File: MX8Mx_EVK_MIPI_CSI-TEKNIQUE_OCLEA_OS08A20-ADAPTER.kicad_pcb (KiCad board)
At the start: 2 copper layers, 40.6 x 40.2 mm, 11 parts, among them J1 1888863-4, J2 XF2M-3215-1A, U1 NLSX5014DTR2G, U2 SN74LVC1G14DRL

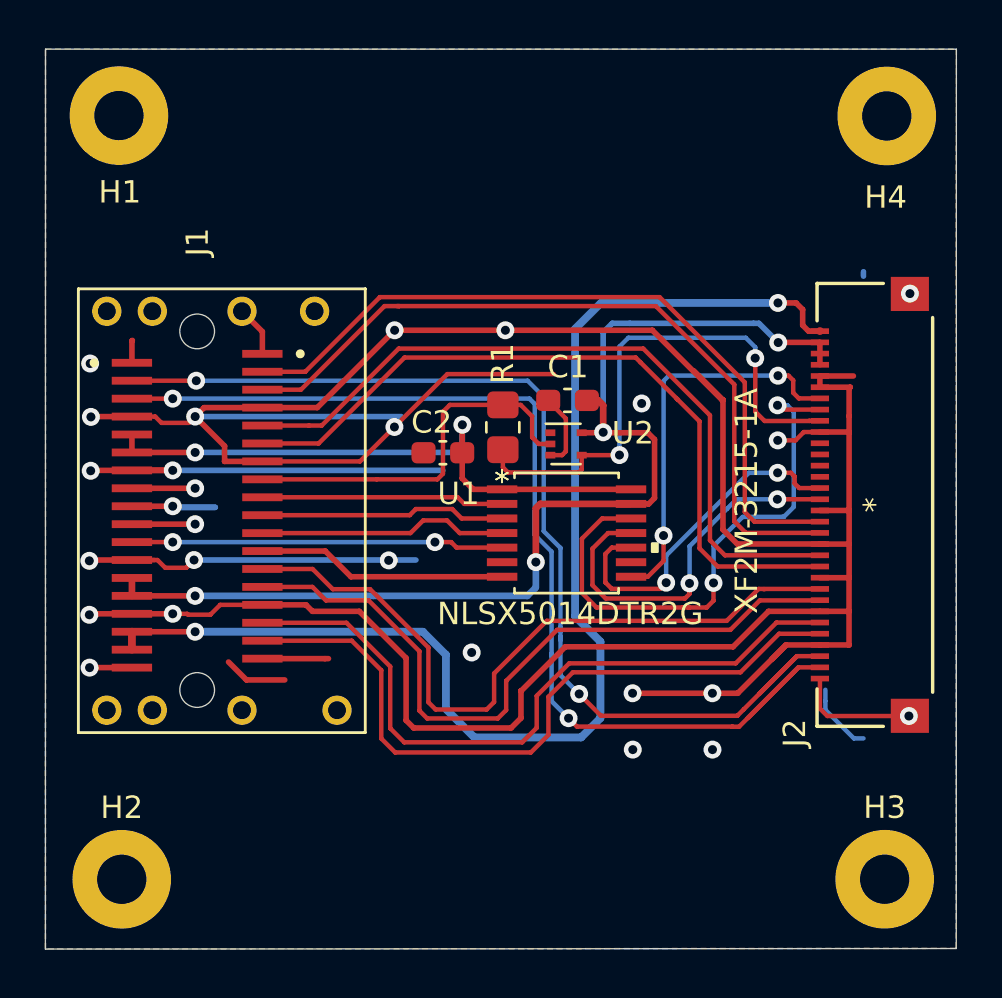
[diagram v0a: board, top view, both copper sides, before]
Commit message: Mirror J1 signals (A-side to B-side and vice-versa) for mating with the MIPI-CSI interface(s) on EVK
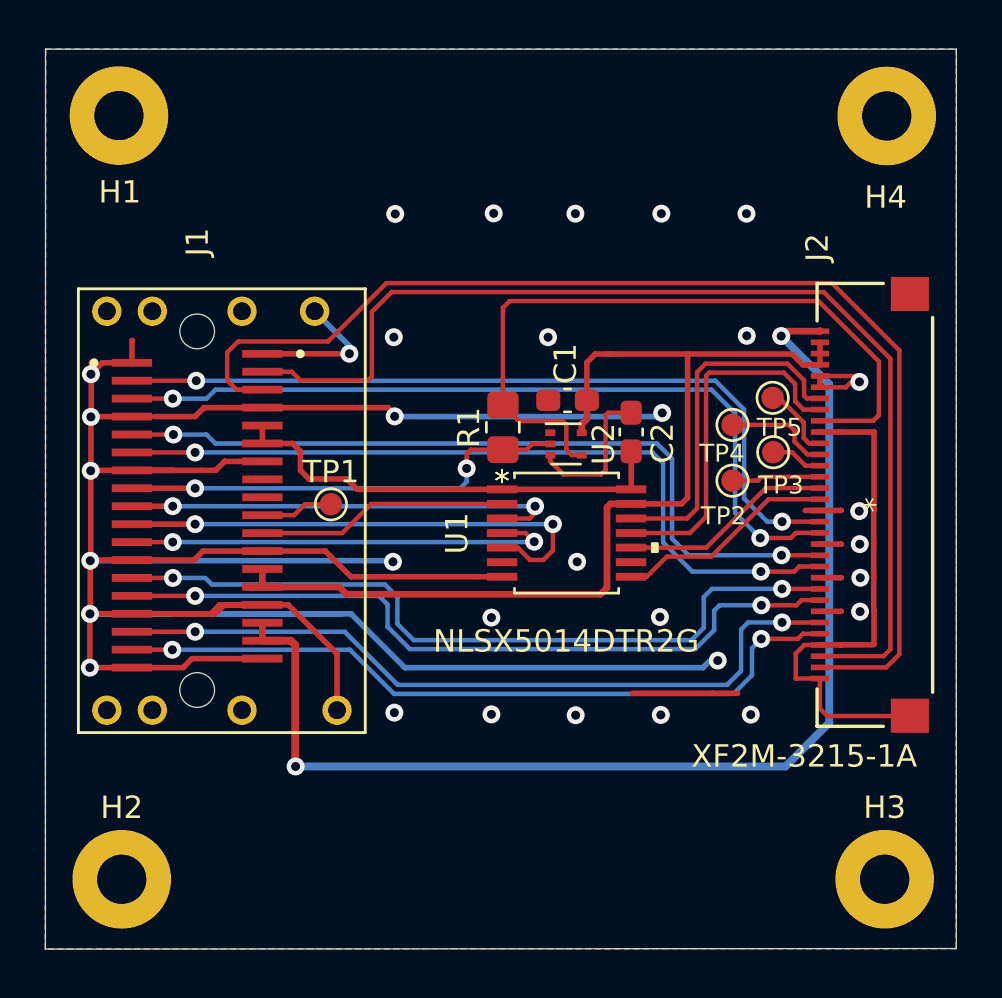
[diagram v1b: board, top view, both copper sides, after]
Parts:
- added TP1: TestPoint, TestPoint:TestPoint_Pad_D1.0mm, F.Cu at (114.8, 96.5)
- added TP2: TestPoint, TestPoint:TestPoint_Pad_D1.0mm, F.Cu at (132.8, 95.5)
- added TP3: TestPoint, TestPoint:TestPoint_Pad_D1.0mm, F.Cu at (134.6, 94.2)
- added TP4: TestPoint, TestPoint:TestPoint_Pad_D1.0mm, F.Cu at (132.8, 93.0)
- added TP5: TestPoint, TestPoint:TestPoint_Pad_D1.0mm, F.Cu at (134.6, 91.8)
- moved C2 8.45 mm to (128.2, 93.3), turned to 90 degrees
- turned R1 to 270 degrees
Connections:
- J1 pad A10: /CSI_SYNC_1V8 -> /I2C_SDA_1V8
- J1 pad A11: /CSI_PWDN_1V8 -> /I2C_SCL_1V8
- J1 pad A13: +3V3 -> /CSI_DN2__SD_LVDS2_N
- J1 pad A14: +3V3 -> /CSI_DP2__SD_LVDS2_P
- J1 pad A16: +5V -> /CSI_DN3__SD_LVDS3_N
- J1 pad A17: +5V -> /CSI_DP3__SD_LVDS3_P
- J1 pad A2: /CSI_CLK_N__SPCLK_LVDS0_N -> /CSI_DN0__SD_LVDS0_N
- J1 pad A3: /CSI_CLK_P__SPCLK_LVDS0_P -> /CSI_DP0__SD_LVDS0_P
- J1 pad A5: +1V8 -> /CSI_DN1__SD_LVDS1_N
- J1 pad A6: +1V8 -> /CSI_DP1__SD_LVDS1_P
- J1 pad A8: Net-(J1-PadA8) -> /CSI_MCLK_1V8
- J1 pad A9: Net-(J1-PadA9) -> /CSI_nRST_1V8
- J1 pad B10: /I2C_SDA_1V8 -> /CSI_SYNC_1V8
- J1 pad B11: /I2C_SCL_1V8 -> /CSI_PWDN_1V8
- J1 pad B13: /CSI_DN2__SD_LVDS2_N -> +3V3
- J1 pad B14: /CSI_DP2__SD_LVDS2_P -> +3V3
- J1 pad B16: /CSI_DN3__SD_LVDS3_N -> +5V
- J1 pad B17: /CSI_DP3__SD_LVDS3_P -> +5V
- J1 pad B2: /CSI_DN0__SD_LVDS0_N -> /CSI_CLK_N__SPCLK_LVDS0_N
- J1 pad B3: /CSI_DP0__SD_LVDS0_P -> /CSI_CLK_P__SPCLK_LVDS0_P
- J1 pad B5: /CSI_DN1__SD_LVDS1_N -> +1V8
- J1 pad B6: /CSI_DP1__SD_LVDS1_P -> +1V8
- J1 pad B8: /CSI_MCLK_1V8 -> Net-(J1-PadB8)
- J1 pad B9: /CSI_nRST_1V8 -> Net-(J1-PadB9)
- U1 pad 11: /I2C_DAT_3V3 -> /SENS_RST_3V3
- U1 pad 12: /SENS_RST_3V3 -> /SENS_EN_3V3
- U1 pad 2: /CSI_nRST_1V8 -> /CSI_PWDN_1V8
- U1 pad 3: /I2C_SDA_1V8 -> /CSI_nRST_1V8
- U1 pad 5: /CSI_PWDN_1V8 -> /I2C_SDA_1V8
- U1 pad 8: /SENS_EN_3V3 -> /I2C_DAT_3V3
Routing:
- net GND: track 213.9 -> 201.8 mm, vias 23 -> 32
- net /I2C_SDA_1V8: track 11.0 -> 22.6 mm, vias 0 -> 2
- net /CSI_nRST_1V8: track 10.8 -> 19.9 mm, vias 0 -> 2
- net /SENS_RST_3V3: track 25.2 -> 16.2 mm, vias 2 -> 0
- net /CLK_SI_3V3: track 23.9 -> 32.6 mm, vias 2 -> 0
- net /I2C_SCL_1V8: track 11.2 -> 19.4 mm, vias 0 -> 2
- net /I2C_DAT_3V3: track 17.1 -> 9.86 mm, vias 2 -> 0
- net +1V8: track 26.8 -> 20.3 mm, vias 2 -> 0
- net +3V3: track 51.8 -> 45.4 mm, vias 4 -> 0
- net /I2C_CLK_3V3: track 15.5 -> 9.53 mm, vias 2 -> 0
- net Net-(J1-PadA9): track 5.54 -> 0.00 mm, vias 1 -> 0
- net /CSI_PWDN_1V8: track 16.6 -> 11.2 mm, vias 2 -> 0
- net /SVSYNC: track 0.00 -> 4.73 mm
- net /CSI_CLK_P__SPCLK_LVDS0_P: track 48.7 -> 52.8 mm, vias 2 -> 0
- net /IRCUT_SW: track 0.00 -> 3.97 mm
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
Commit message: Change 32-pin connector from Omron XF2M-3215-1A to TE 3-1734592-2
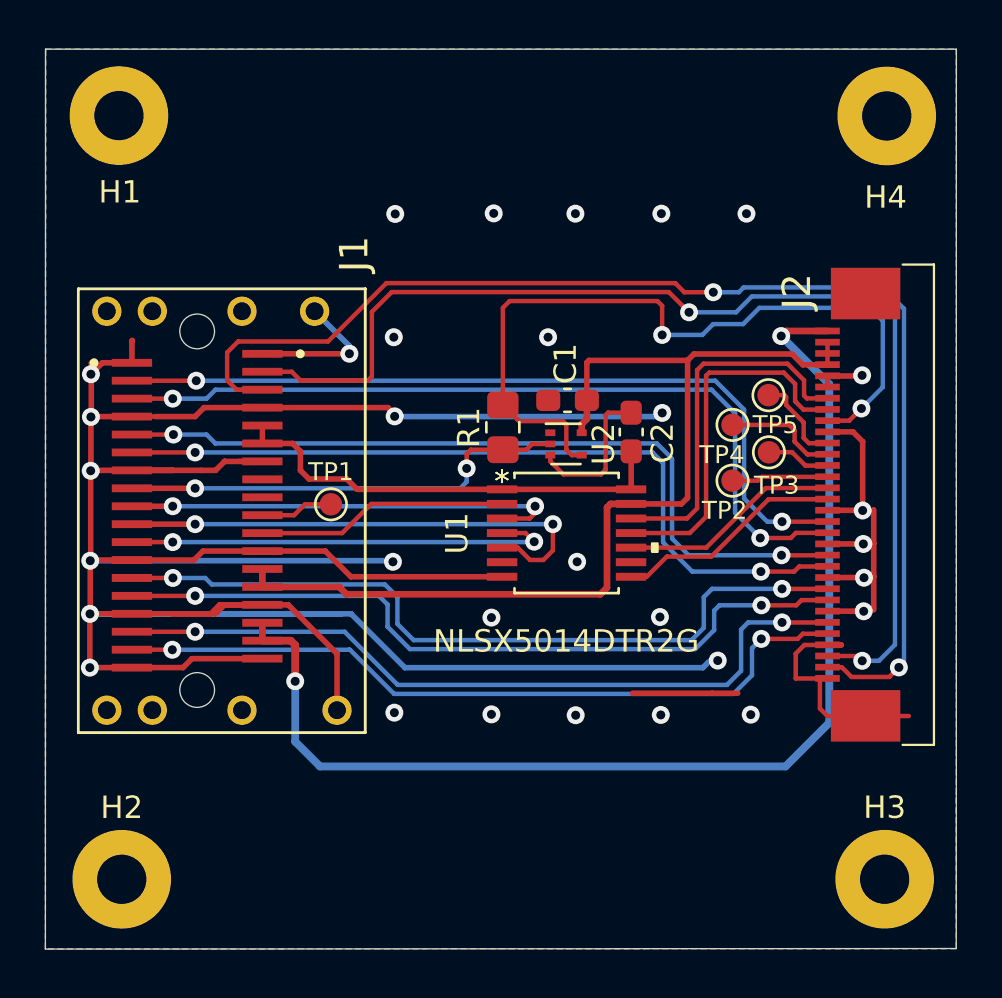
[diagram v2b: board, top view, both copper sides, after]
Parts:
- J2: value XF2M-3215-1A -> 3-1734592-2; footprint footprints:XF2M-3215-1A -> footprints:317345922
- moved J2 1.76 mm to (137.4, 96.5), turned to 90 degrees
- moved TP5 0.22 mm to (134.4, 91.6)
- moved TP3 0.19 mm to (134.4, 94.2)
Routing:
- net GND: track 201.8 -> 197.8 mm, vias 32 -> 31
- net /CLK_SI_3V3: track 32.6 -> 34.7 mm, vias 0 -> 2
- net /CSI_CLK_P__SPCLK_LVDS0_P: track 52.8 -> 54.8 mm, vias 0 -> 2
- net /CSI_CLK_N__SPCLK_LVDS0_N: track 49.0 -> 50.8 mm, vias 0 -> 2

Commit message: Add round-corners
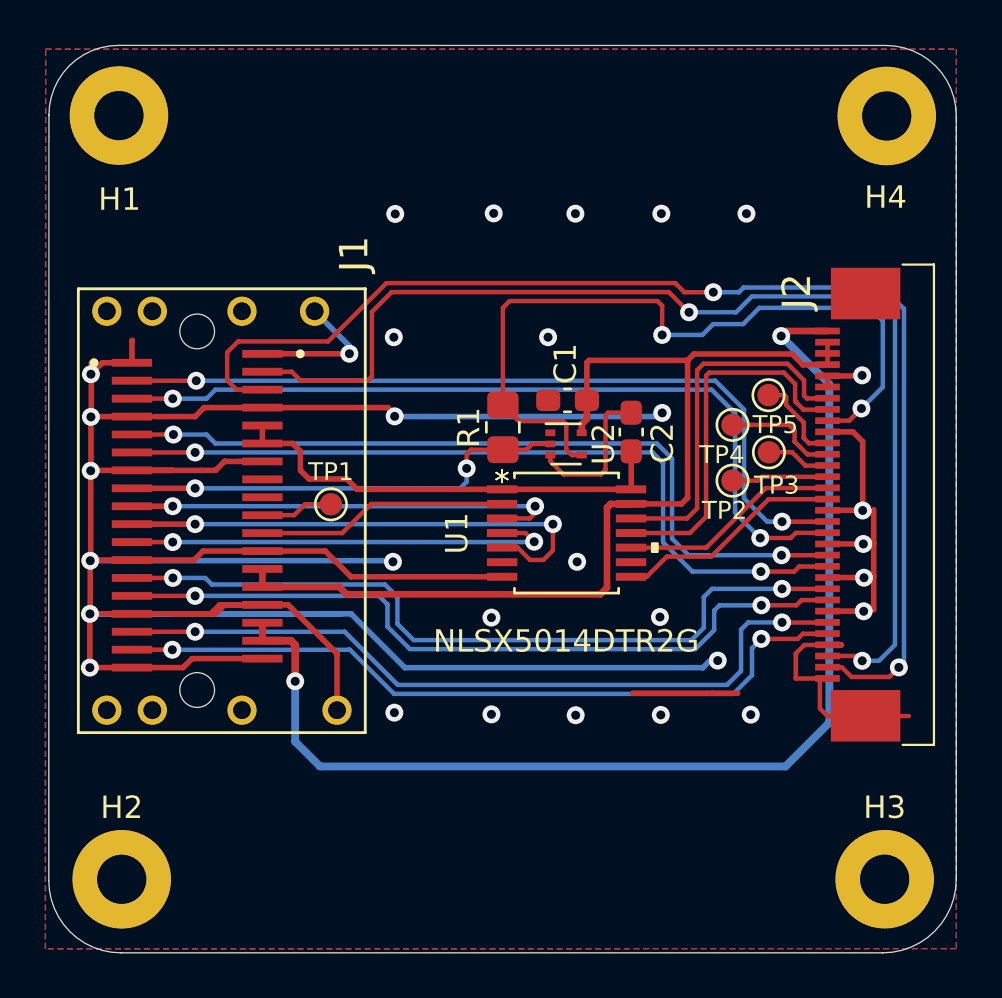
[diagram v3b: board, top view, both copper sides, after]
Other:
- board size 40.6 x 40.2 mm -> 40.5 x 40.5 mm

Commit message: Update V1A revision
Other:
- board text added: "OCLEA OS08a20 Rev. V1A"

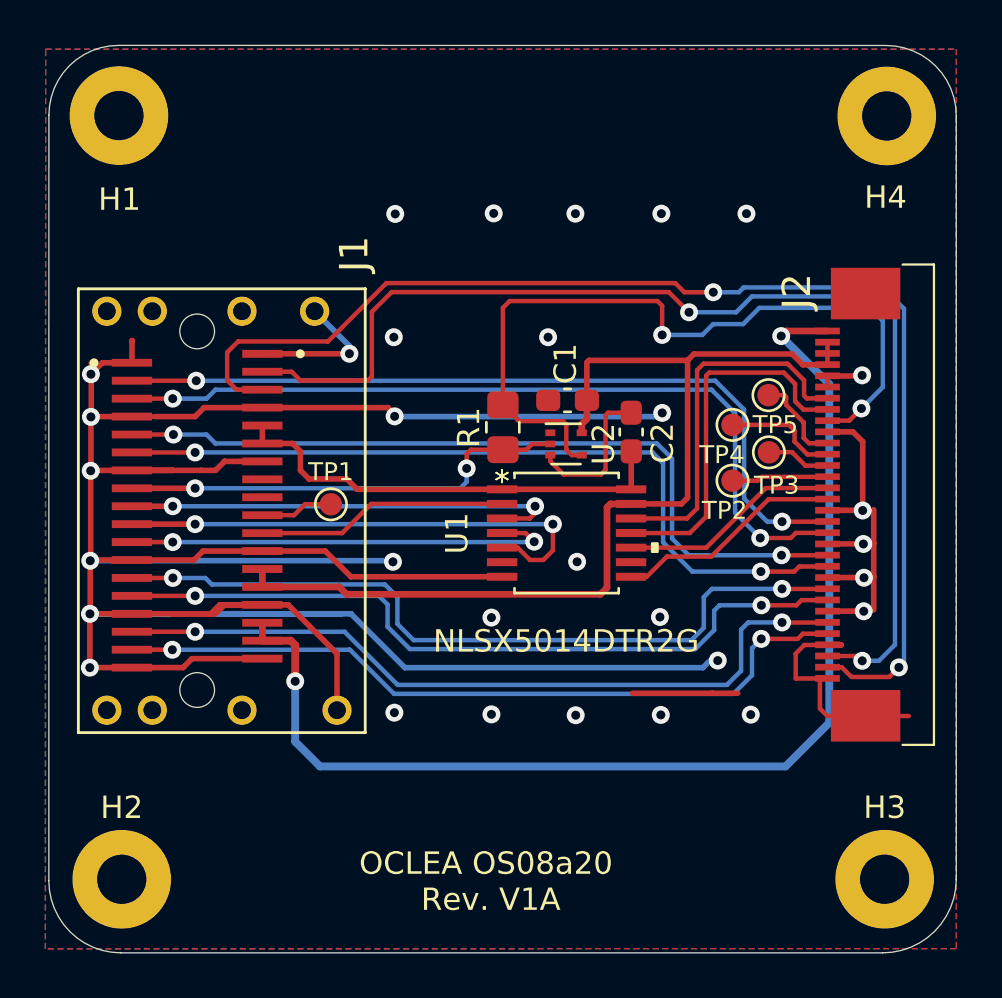
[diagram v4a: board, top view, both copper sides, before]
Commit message: Complete routing of new design with separate I2C and GPIO level translators
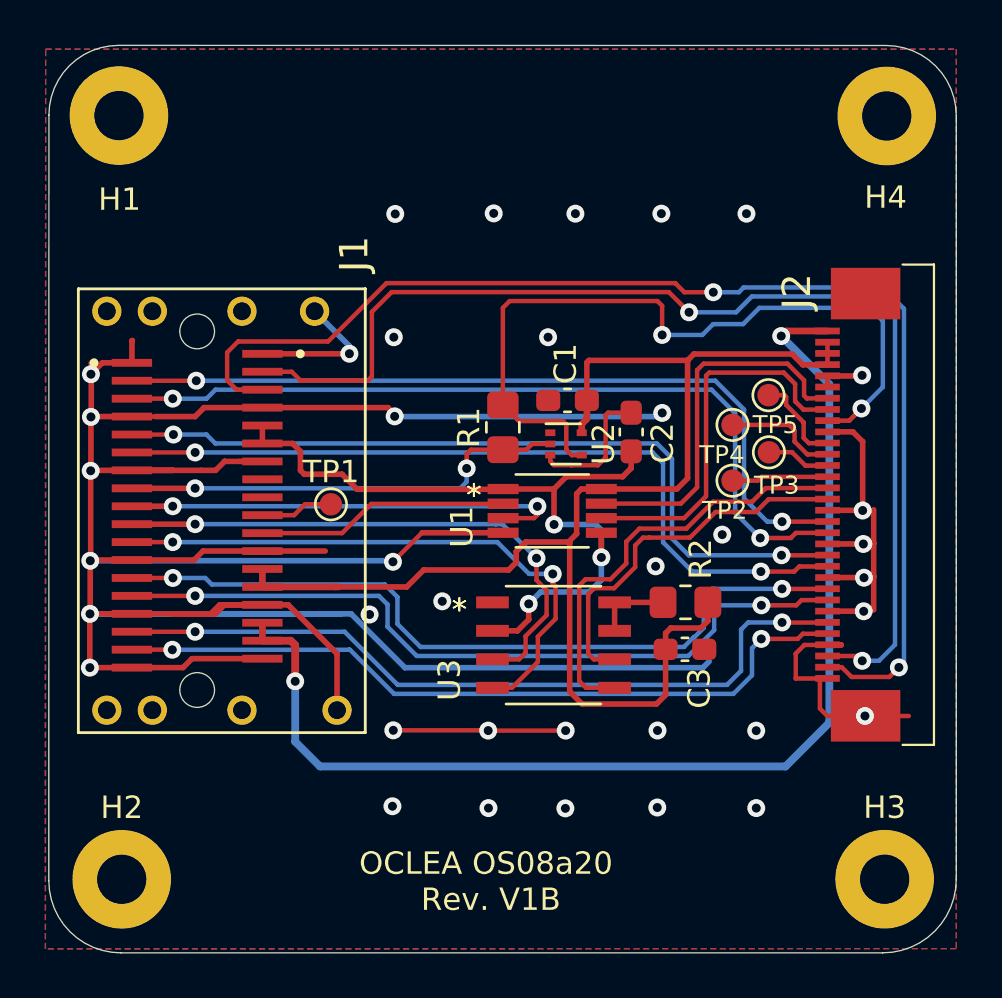
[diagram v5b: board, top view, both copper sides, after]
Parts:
- added C3: C, Capacitor_SMD:C_0603_1608Metric_Pad1.08x0.95mm_HandSolder, F.Cu at (130.6, 103.0)
- added R2: 200K, Resistor_SMD:R_0805_2012Metric_Pad1.20x1.40mm_HandSolder, F.Cu at (130.7, 100.9)
- added U3: PCA9306D, footprints:PCA9306D, F.Cu at (124.8, 102.8)
- U1: value NLSX5014DTR2G -> NLSX5012DMR2G; footprint footprints:NLSX5014DTR2G -> footprints:NLSX5012DMR2G
- moved U1 1.18 mm to (124.7, 96.8)
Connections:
- U1 pad 4: /I2C_SCL_1V8 -> GND
- U1 pad 5: /I2C_SDA_1V8 -> +1V8
- U1 pad 6: Net-(U1-Pad6) -> /SENS_RST_3V3
- U1 pad 7: GND -> /SENS_EN_3V3
- U1 pad 8: /I2C_DAT_3V3 -> +3V3
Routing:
- net +3V3: track 44.9 -> 60.6 mm
- net +1V8: track 20.3 -> 33.0 mm, vias 0 -> 3
- net /I2C_CLK_3V3: track 9.53 -> 19.1 mm
- net /I2C_DAT_3V3: track 9.86 -> 16.6 mm
- net /I2C_SCL_1V8: track 19.4 -> 26.2 mm
- net Net-(R2-Pad2): track 0.00 -> 3.43 mm
- net /I2C_SDA_1V8: track 22.6 -> 25.1 mm
- net GND: track 197.8 -> 197.3 mm, vias 31 -> 37
- net /SENS_RST_3V3: track 16.2 -> 16.7 mm
- net /SENS_EN_3V3: track 15.9 -> 16.4 mm
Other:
- board text added: "OCLEA OS08a20 Rev. V1B"
- board text removed: "OCLEA OS08a20 Rev. V1A"
